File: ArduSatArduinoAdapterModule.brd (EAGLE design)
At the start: 95.5 x 90.3 mm, 28 parts, among them J1 Power, J2 Analog, J3 D8_13, J4 D0_7, J5 M17, J6 M17, U1 ICSP, U2 ICSP-Breakout

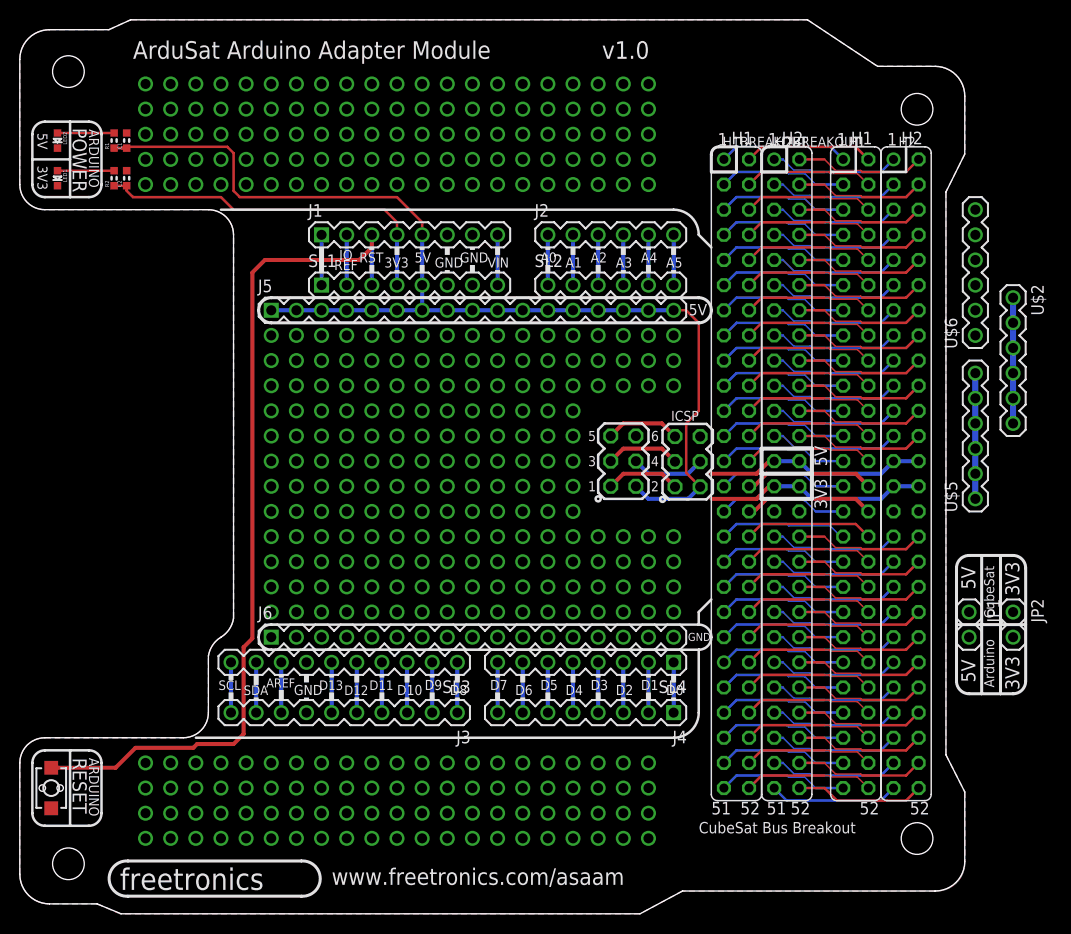
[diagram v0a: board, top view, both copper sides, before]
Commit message: Switched to 4 layer PCB; completed all routing
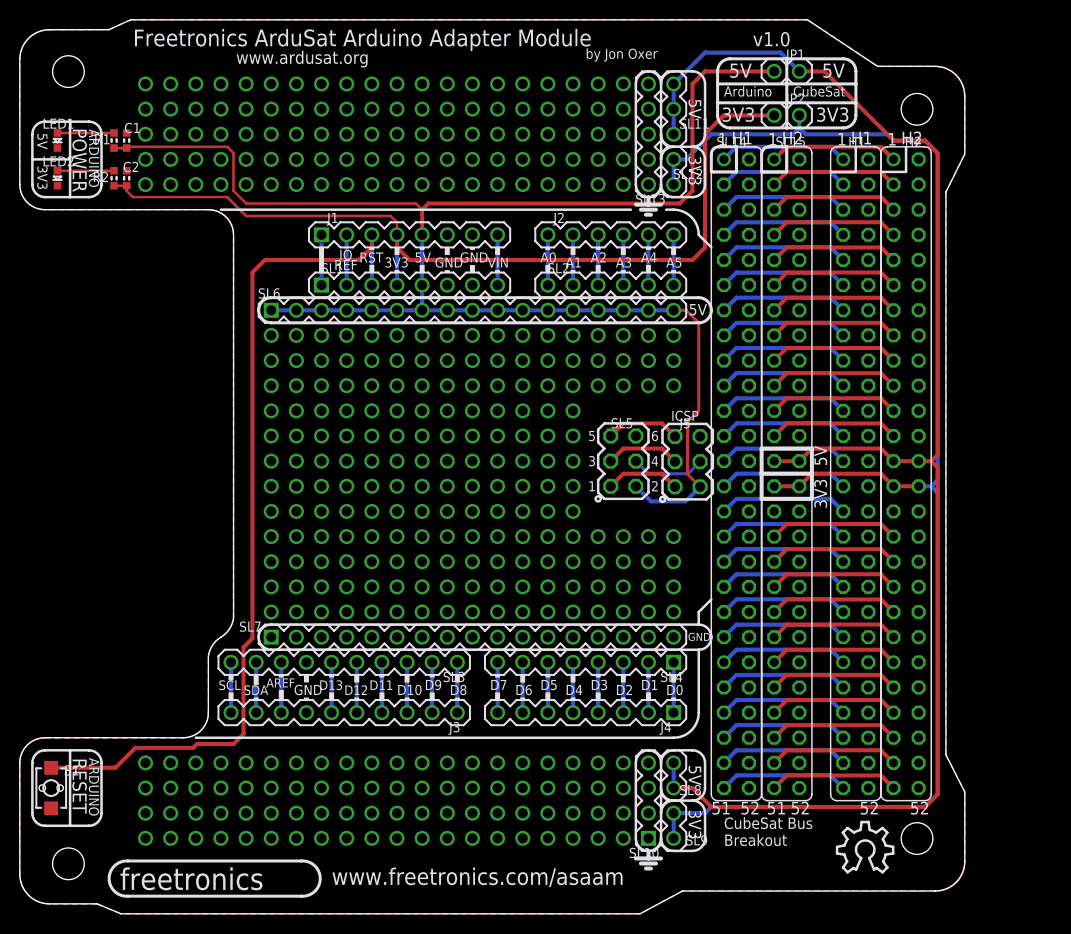
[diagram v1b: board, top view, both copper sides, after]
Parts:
- removed U$2: (no value), freetronics-original:1X06
- removed U1: ICSP, freetronics-jon:2X03PTH
- added SL10: (no value), freetronics-master-v1.1:1X04
- added SL11: (no value), freetronics-master-v1.1:1X03
- added SL12, SL8, SL9: (no value), freetronics-master-v1.1:1X02
- added SL13: (no value), freetronics-master-v1.1:1X05
- added SL6: M17, freetronics-master-v1.1:1X17
- J5: value M17 -> ICSP; device freetronics-master-v1.1:1X17 -> freetronics-jon:2X03PTH
- LED1: value JADEGREEN 0603 -> BLUE 0603
- LED2: value BLUE 0603 -> JADEGREEN 0603
- R1: value 2K2 -> 2K2 0603
- R2: value 1K -> 1K 0603
- SL14: value CUBESATBUSH -> H1BREAKOUT
- SL15: value CUBESATBUSH -> H2BREAKOUT
- U$5, U$6: device freetronics-original:1X06 -> OSHW:OSHW_10X200_NOTEXT
- moved JP1 57.2 mm to (78.7, 85.1), turned to 180 degrees
- moved U$6 56.0 mm to (82.5, 4.19), turned to 0 degrees
- moved JP2 54.6 mm to (78.7, 80.6), turned to 180 degrees
- moved J5 44.7 mm to (67.5, 45.7), flipped to the bottom, turned to 90 degrees
- moved U$5 39.4 mm to (85.1, 4.19), flipped to the bottom, turned to 0 degrees
- moved LED1 3.81 mm to (3.81, 78.1)
- moved LED2 3.81 mm to (3.81, 74.3)
- renumbered H1BREAKOUT to SL14, H2BREAKOUT to SL15, J6 to SL7, U2 to SL5
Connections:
- net +5V_SYS: now also SL11.1, SL11.2, SL11.3, SL8.1, SL8.2; no longer U$2.1, U$2.2, U$2.3, U$2.4, U$2.5, U$2.6
- net 5V: now also SL6.1, SL6.10, SL6.11, SL6.12, SL6.13, SL6.14, SL6.15, SL6.16, SL6.17, SL6.2, SL6.3, SL6.4, SL6.5, SL6.6, SL6.7, SL6.8, SL6.9; no longer J5.1, J5.10, J5.11, J5.12, J5.13, J5.14, J5.15, J5.16, J5.17, J5.3, J5.4, J5.5, J5.6, J5.7, J5.8, J5.9, U1.2
- net GND: now also J5.6, SL10.1, SL10.2, SL10.3, SL10.4, SL13.1, SL13.2, SL13.3, SL13.4, SL13.5; no longer U$6.1, U$6.2, U$6.3, U$6.4, U$6.5, U$6.6, U1.6
- net N$1: now also LED2.A; no longer LED1.A
- net N$35: now also J5.4; no longer U1.4
- net N$51: now also J5.1; no longer U1.1
- net N$52: now also J5.3; no longer U1.3
- net N$53: now also J5.5; no longer U1.5
- net N$6: now also LED1.A; no longer LED2.A
- net VCC_SYS: now also SL12.1, SL12.2, SL9.1, SL9.2; no longer U$5.1, U$5.2, U$5.3, U$5.4, U$5.5, U$5.6
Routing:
- net +5V_SYS: track 35.2 -> 150.0 mm
- net VCC_SYS: track 35.2 -> 145.1 mm
- net 3V3: track 36.7 -> 89.4 mm
- net 5V: track 115.3 -> 163.8 mm
- net GND: track 13.1 -> 0.00 mm
- added copper zone on layer 15, net GND
- added copper zone on layer 2, net GND
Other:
- board text added: "Copyright 2012 Freetronics Pty Ltd www.freetronics.com/asaam SKU: ASAAM"
- board text added: "Freetronics ArduSat Arduino Adapter Module"
- board text added: "ROHS"
- board text added: "Released under the TAPR Open Hardware License www.tapr.org/OHL"
- board text added: "S1"
- board text added: "by Jon Oxer"
- board text added: "www.ardusat.org"
- board text removed: "(c) 2012 Freetronics Pty Ltd"
- board text removed: "ArduSat Arduino Adapter Module"

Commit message: Added grounded corner mount holes and relocated some traces to inner layers to minimise risk of shorts to mounting sleeves
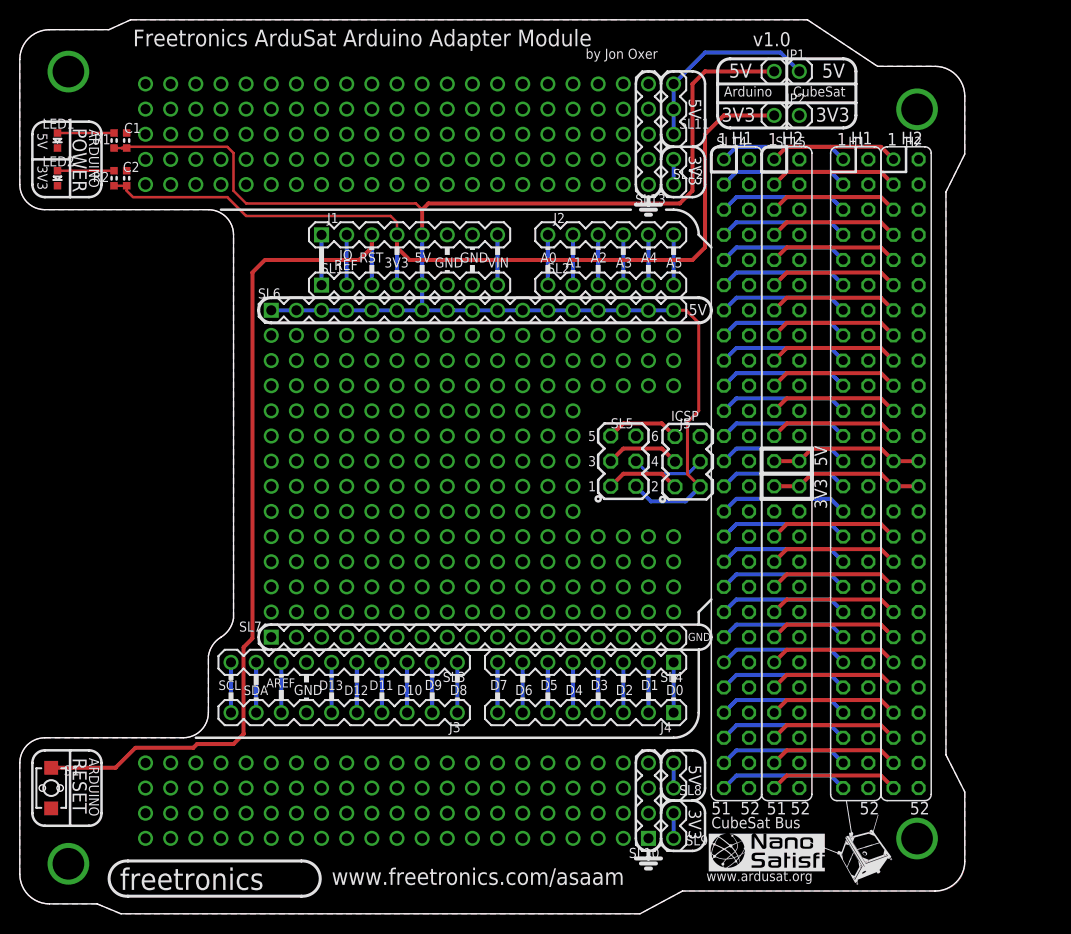
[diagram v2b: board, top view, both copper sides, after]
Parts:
- removed U$6: (no value), OSHW:OSHW_10X200_NOTEXT
- added MNT1, MNT2, MNT3, MNT4: HOLE3.2MM, freetronics-jon:HOLE32
- JP1: value (none) -> 5V-LINK
- JP2: value (none) -> 3V3-LINK
- SL10, SL13: value (none) -> GND
- SL11, SL8: value (none) -> +5V_SYS
- SL12, SL9: value (none) -> VCC_SYS
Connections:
- net H1L41 renamed SDA_SYS
- net H1L43 renamed SCL_SYS
- net H2L45 renamed VBATT45
- net H2L49 renamed SDA2
- net H2L51 renamed SCL2
- net H2R46 renamed VBATT46
- net GND: now also MNT1.P$1, MNT2.P$1, MNT3.P$1, MNT4.P$1
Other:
- board text added: "/Users/jon/Dropbox/Freetronics/ConsultingProjects/ArduSat/nanosatisfi 2-2 BW.bmp"
- board text added: "CubeSat Bus"
- board text removed: "CubeSat Bus Breakout"
